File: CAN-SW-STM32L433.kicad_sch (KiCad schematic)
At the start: 37 parts, among them J1 H GND L, J2 TERM, J3 UART1, J4 SWLINK, J5 CENTER +12V, U1 STM32L433RCT3, U2 MCP2562-E-SN

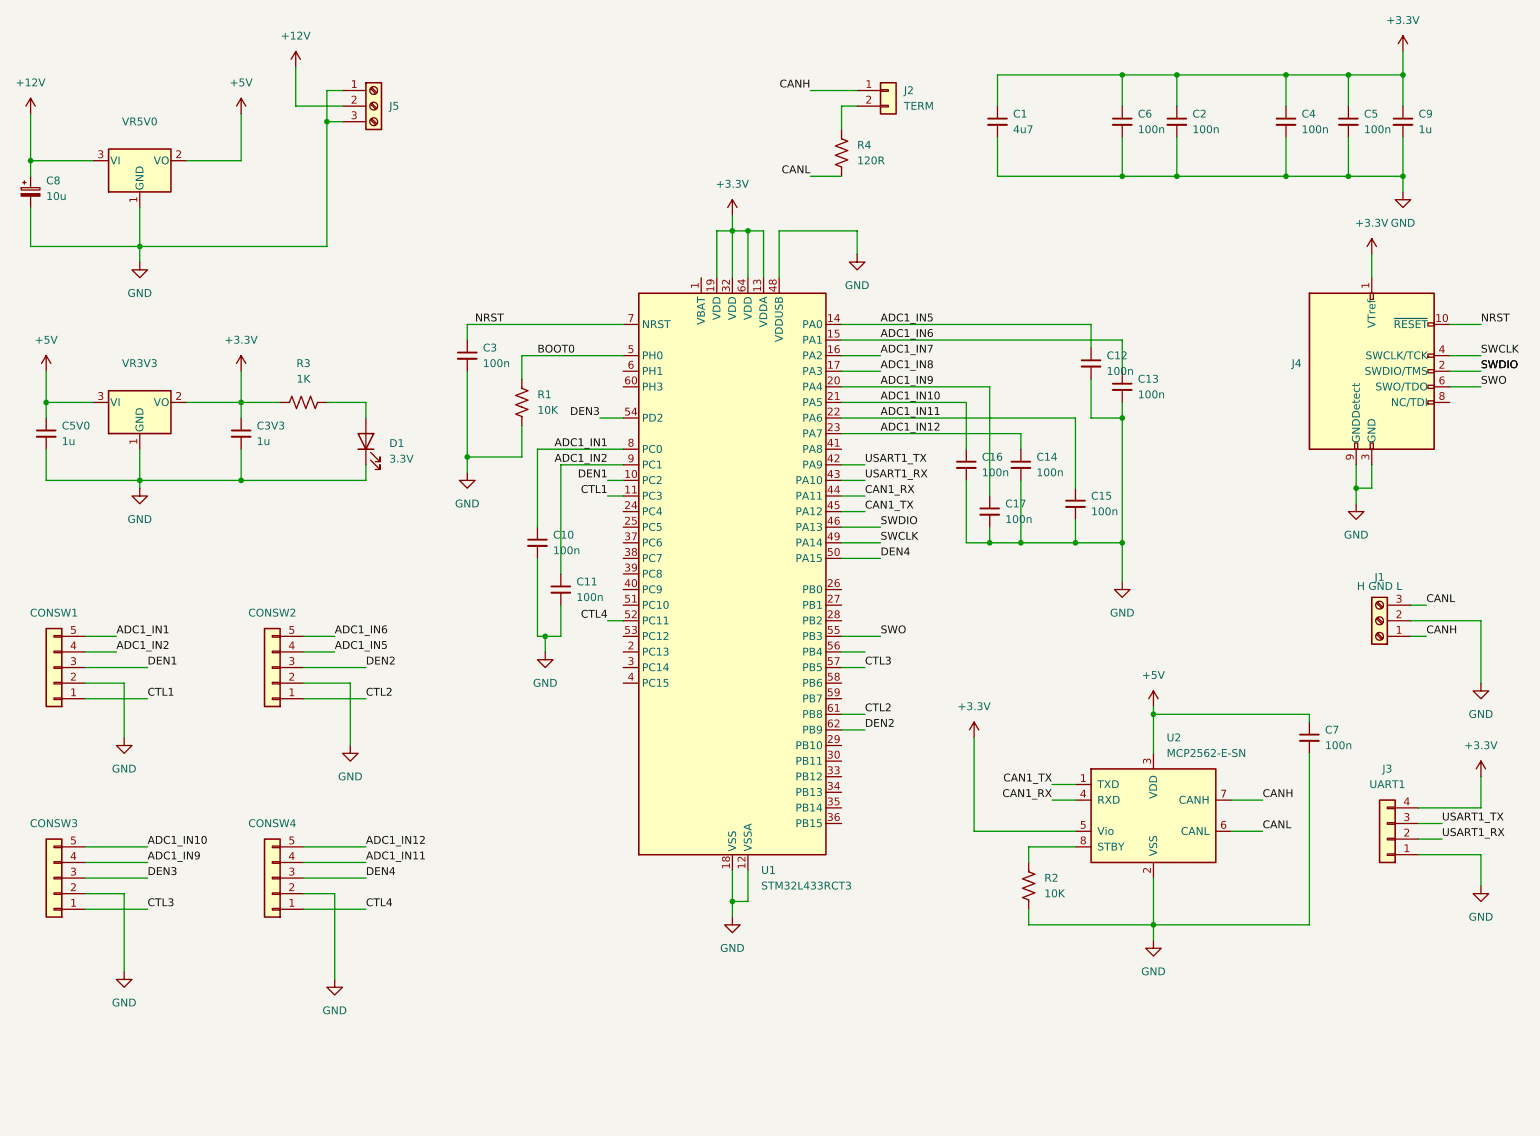
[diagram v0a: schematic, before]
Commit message: added status led and tvs diode
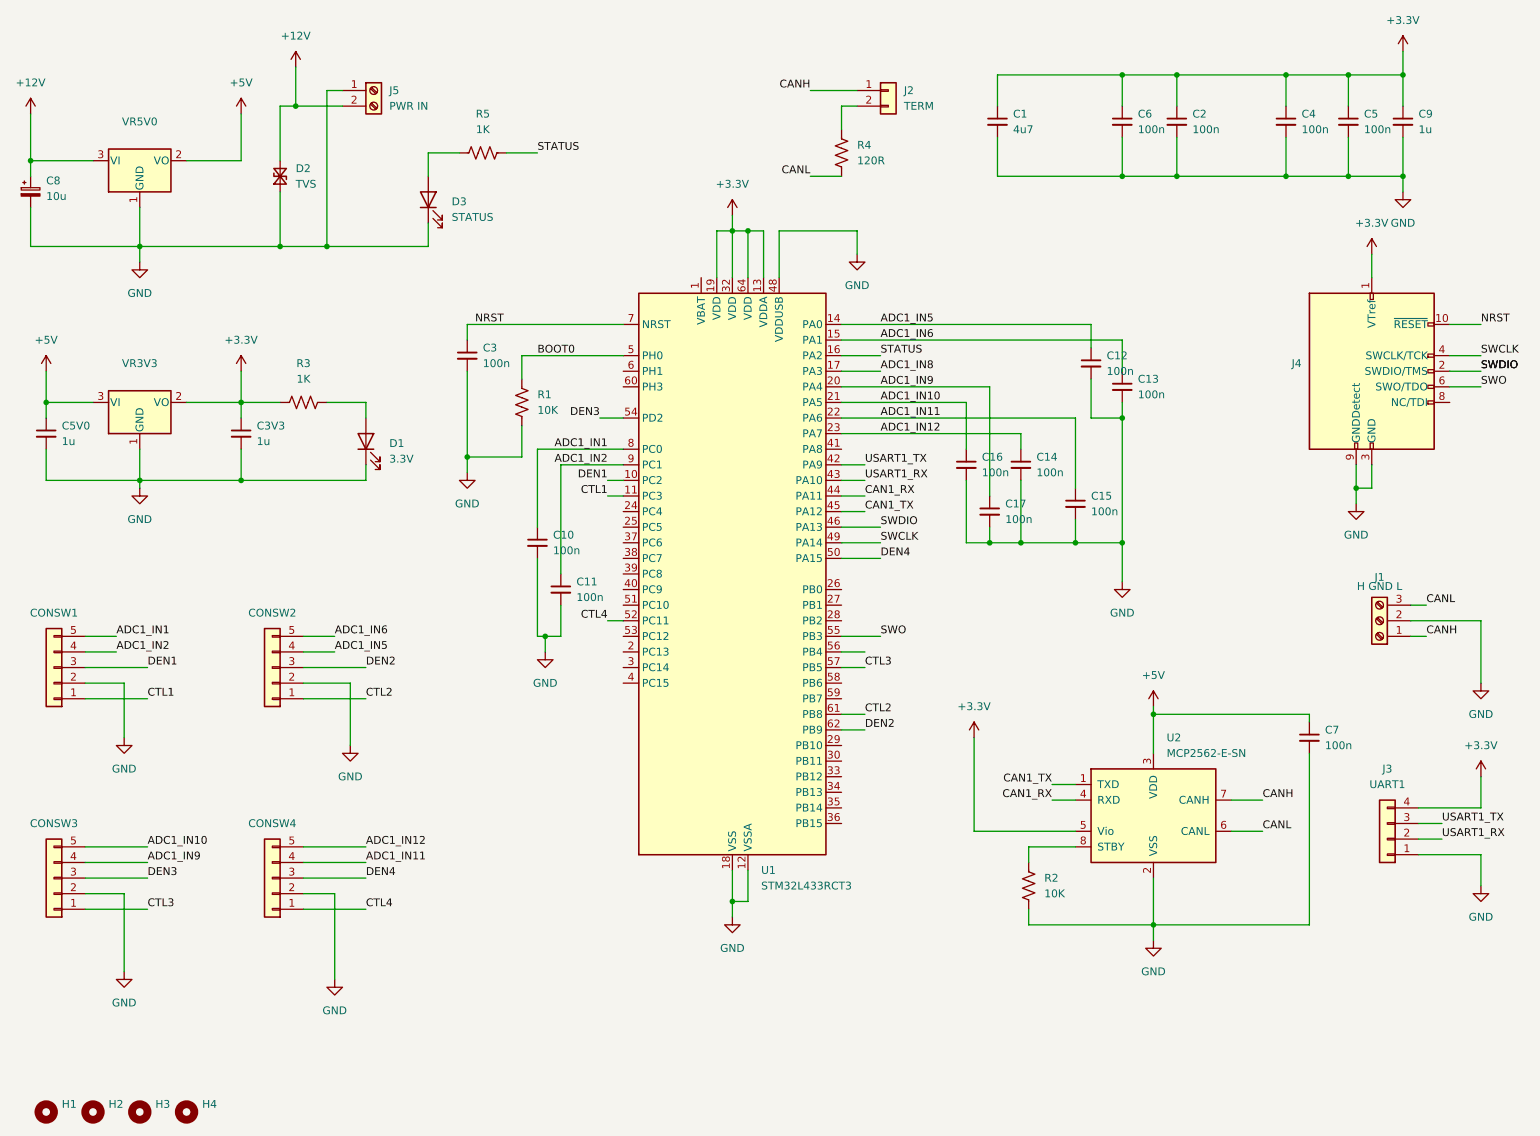
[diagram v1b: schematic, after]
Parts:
- removed J5: CENTER +12V, TerminalBlock_Phoenix:TerminalBlock_Phoenix_MKDS-1,5-3_1x03_P5.00mm_Horizontal, symbol Connector:Screw_Terminal_01x03
- added D2: TVS, Diode_SMD:D_0603_1608Metric_Pad1.05x0.95mm_HandSolder, symbol Device:D_TVS_Small
- added D3: STATUS, LED_THT:LED_D5.0mm_Clear, symbol Device:LED
- added H1, H2, H3, H4: MountingHole, MountingHole:MountingHole_3.2mm_M3_DIN965, symbol Mechanical:MountingHole
- added J5: PWR IN, TerminalBlock_Phoenix:TerminalBlock_Phoenix_MKDS-1,5-2_1x02_P5.00mm_Horizontal, symbol Connector:Screw_Terminal_01x02
- added R5: 1K, Resistor_SMD:R_0603_1608Metric_Pad0.98x0.95mm_HandSolder, symbol Device:R_US
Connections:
- net +12V: now also D2.2 (A2), J5.2 (Pin_2)
- net GND: now also D2.1 (A1), D3.1 (K), J5.1 (Pin_1)
- net ADC1_IN7 renamed STATUS
- net STATUS: now also R5.2
- new net: D3.2 (A), R5.1

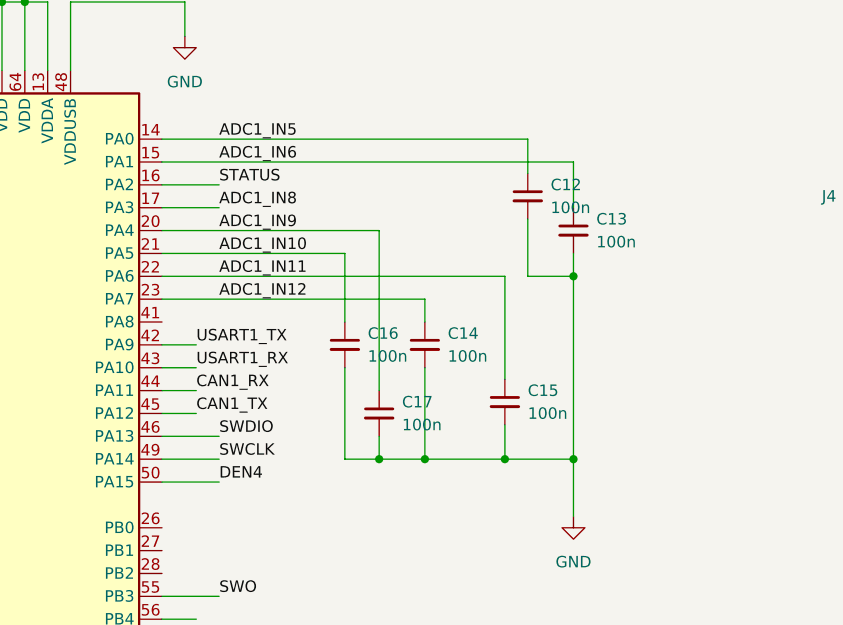
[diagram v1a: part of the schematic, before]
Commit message: fix TVS package size, do some layout tweaks
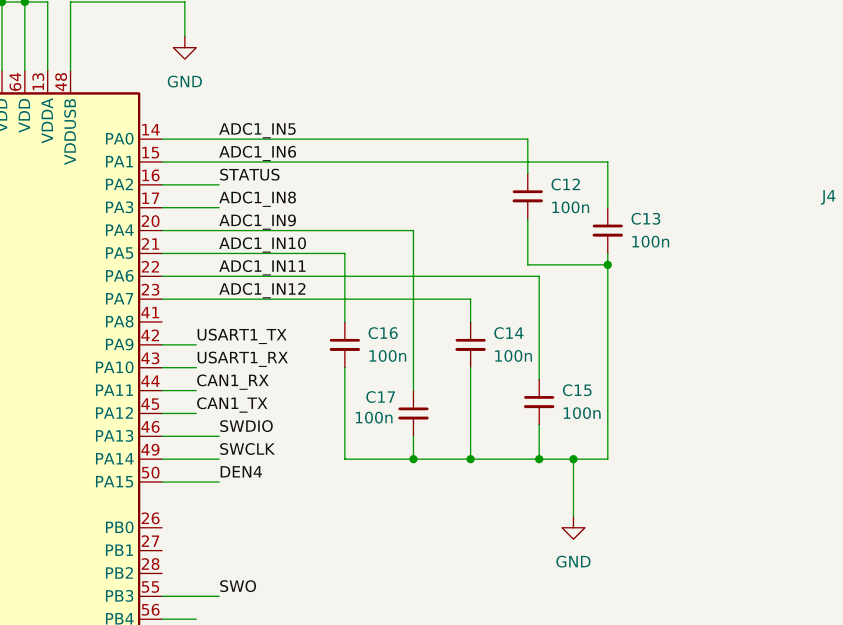
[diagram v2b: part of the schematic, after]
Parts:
- D2: footprint Diode_SMD:D_0603_1608Metric_Pad1.05x0.95mm_HandSolder -> Diode_SMD:D_SMA_Handsoldering
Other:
- moved on the sheet: C13, C14, C15, C17
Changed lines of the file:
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@@
 	)
 	(junction
-		(at 195.58 96.52)
+		(at 212.09 36.83)
 		(diameter 0)
 		(color 0 0 0 0)
 	)
 	(junction
-		(at 212.09 36.83)
+		(at 208.28 158.75)
 		(diameter 0)
 		(color 0 0 0 0)
 	)
 	(junction
-		(at 208.28 158.75)
+		(at 25.4 34.29)
 		(diameter 0)
 		(color 0 0 0 0)
 	)
 	(junction
-		(at 25.4 34.29)
+		(at 191.77 96.52)
 		(diameter 0)
 		(color 0 0 0 0)
@@
 	)
 	(junction
-		(at 68.58 25.4)
+		(at 185.42 96.52)
 		(diameter 0)
 		(color 0 0 0 0)
 	)
 	(junction
-		(at 186.69 96.52)
+		(at 68.58 25.4)
 		(diameter 0)
 		(color 0 0 0 0)
@@
 	)
 	(junction
+		(at 199.39 96.52)
+		(diameter 0)
+		(color 0 0 0 0)
+	)
+	(junction
 		(at 212.09 20.32)
 		(diameter 0)
@@
 	)
 	(junction
-		(at 181.61 96.52)
-		(diameter 0)
-		(color 0 0 0 0)
-	)
-	(junction
-		(at 203.2 76.2)
+		(at 207.01 74.93)
 		(diameter 0)
 		(color 0 0 0 0)
@@
 	(wire
 		(pts
-			(xy 181.61 71.12) (xy 181.61 88.9)
+			(xy 185.42 71.12) (xy 185.42 88.9)
 		)
 		(stroke
@@
 	(wire
 		(pts
-			(xy 203.2 73.66) (xy 203.2 76.2)
+			(xy 207.01 73.66) (xy 207.01 74.93)
 		)
 		(stroke
@@
 	(wire
 		(pts
+			(xy 191.77 96.52) (xy 199.39 96.52)
+		)
+		(stroke
+			(width 0)
+			(type default)
+		)
+	)
+	(wire
+		(pts
 			(xy 261.62 109.22) (xy 250.19 109.22)
 		)
@@
 	(wire
 		(pts
-			(xy 181.61 96.52) (xy 177.8 96.52)
+			(xy 177.8 96.52) (xy 185.42 96.52)
 		)
 		(stroke
@@
 	(wire
 		(pts
+			(xy 199.39 96.52) (xy 203.2 96.52)
+		)
+		(stroke
+			(width 0)
+			(type default)
+		)
+	)
+	(wire
+		(pts
 			(xy 157.48 124.46) (xy 161.29 124.46)
 		)
@@
 	(wire
 		(pts
+			(xy 207.01 96.52) (xy 203.2 96.52)
+		)
+		(stroke
+			(width 0)
+			(type default)
+		)
+	)
+	(wire
+		(pts
 			(xy 240.03 20.32) (xy 248.92 20.32)
 		)
@@
 	(wire
 		(pts
-			(xy 195.58 76.2) (xy 195.58 87.63)
+			(xy 199.39 76.2) (xy 199.39 87.63)
 		)
 		(stroke
@@
 	(wire
 		(pts
-			(xy 157.48 76.2) (xy 195.58 76.2)
+			(xy 157.48 76.2) (xy 199.39 76.2)
 		)
 		(stroke
@@
 	(wire
 		(pts
-			(xy 203.2 76.2) (xy 203.2 96.52)
-		)
-		(stroke
-			(width 0)
-			(type default)
-		)
-	)
-	(wire
-		(pts
 			(xy 147.32 53.34) (xy 147.32 45.72)
 		)
@@
 	(wire
 		(pts
-			(xy 157.48 78.74) (xy 186.69 78.74)
+			(xy 157.48 78.74) (xy 191.77 78.74)
 		)
 		(stroke
@@
 	(wire
 		(pts
-			(xy 195.58 92.71) (xy 195.58 96.52)
+			(xy 199.39 92.71) (xy 199.39 96.52)
 		)
 		(stroke
@@
 	(wire
 		(pts
+			(xy 185.42 96.52) (xy 191.77 96.52)
+		)
+		(stroke
+			(width 0)
+			(type default)
+		)
+	)
+	(wire
+		(pts
 			(xy 139.7 154.94) (xy 142.24 154.94)
 		)
@@
 	(wire
 		(pts
-			(xy 186.69 86.36) (xy 186.69 96.52)
+			(xy 191.77 86.36) (xy 191.77 96.52)
 		)
 		(stroke
@@
 	(wire
 		(pts
-			(xy 186.69 96.52) (xy 181.61 96.52)
-		)
-		(stroke
-			(width 0)
-			(type default)
-		)
-	)
-	(wire
-		(pts
 			(xy 40.64 153.67) (xy 40.64 166.37)
 		)
@@
 	(wire
 		(pts
-			(xy 198.12 76.2) (xy 203.2 76.2)
+			(xy 198.12 74.93) (xy 207.01 74.93)
 		)
 		(stroke
@@
 	(wire
 		(pts
-			(xy 157.48 71.12) (xy 181.61 71.12)
+			(xy 157.48 71.12) (xy 185.42 71.12)
 		)
 		(stroke
@@
 	(wire
 		(pts
-			(xy 186.69 78.74) (xy 186.69 81.28)
+			(xy 191.77 78.74) (xy 191.77 81.28)
 		)
 		(stroke
@@
 	(wire
 		(pts
-			(xy 181.61 93.98) (xy 181.61 96.52)
+			(xy 185.42 93.98) (xy 185.42 96.52)
 		)
 		(stroke
@@
 	(wire
 		(pts
-			(xy 198.12 69.85) (xy 198.12 76.2)
+			(xy 198.12 69.85) (xy 198.12 74.93)
 		)
 		(stroke
@@
 	(wire
 		(pts
-			(xy 195.58 96.52) (xy 203.2 96.52)
-		)
-		(stroke
-			(width 0)
-			(type default)
-		)
-	)
-	(wire
-		(pts
 			(xy 229.87 36.83) (xy 240.03 36.83)
 		)
@@
 	(wire
 		(pts
-			(xy 186.69 96.52) (xy 195.58 96.52)
+			(xy 207.01 74.93) (xy 207.01 96.52)
 		)
 		(stroke
@@
 	(wire
 		(pts
-			(xy 203.2 68.58) (xy 203.2 63.5)
+			(xy 207.01 68.58) (xy 207.01 63.5)
 		)
 		(stroke
@@
 	(wire
 		(pts
-			(xy 157.48 63.5) (xy 203.2 63.5)
+			(xy 157.48 63.5) (xy 207.01 63.5)
 		)
 		(stroke
@@
 	(symbol
 		(lib_id "Device:C_Small")
-		(at 203.2 71.12 0)
+		(at 207.01 71.12 0)
 		(unit 1)
 		(exclude_from_sim no)
@@
 		(on_board yes)
 		(dnp no)
-		(fields_autoplaced yes)
 		(property "Reference" "C13"
-			(at 205.74 69.8562 0)
+			(at 209.55 69.8562 0)
 			(effects
 				(font
@@
 		)
 		(property "Value" "100n"
-			(at 205.74 72.3962 0)
+			(at 209.55 72.3962 0)
 			(effects
 				(font
@@
 		)
 		(property "Footprint" "Capacitor_SMD:C_0603_1608Metric_Pad1.08x0.95mm_HandSolder"
-			(at 203.2 71.12 0)
+			(at 207.01 71.12 0)
 			(effects
 				(font
@@
 		)
 		(property "Datasheet" "~"
-			(at 203.2 71.12 0)
+			(at 207.01 71.12 0)
 			(effects
 				(font
@@
 		)
 		(property "Description" "Unpolarized capacitor, small symbol"
-			(at 203.2 71.12 0)
+			(at 207.01 71.12 0)
 			(effects
 				(font
@@
 	(symbol
 		(lib_id "Device:C_Small")
-		(at 186.69 83.82 0)
+		(at 191.77 83.82 0)
 		(unit 1)
 		(exclude_from_sim no)
@@
 		(dnp no)
 		(property "Reference" "C14"
-			(at 189.23 82.5562 0)
+			(at 194.31 82.5562 0)
 			(effects
 				(font
@@
 		)
 		(property "Value" "100n"
-			(at 189.23 85.0962 0)
+			(at 194.31 85.0962 0)
 			(effects
 				(font
@@
 		)
 		(property "Footprint" "Capacitor_SMD:C_0603_1608Metric_Pad1.08x0.95mm_HandSolder"
-			(at 186.69 83.82 0)
+			(at 191.77 83.82 0)
 			(effects
 				(font
@@
 		)
 		(property "Datasheet" "~"
-			(at 186.69 83.82 0)
+			(at 191.77 83.82 0)
 			(effects
 				(font
@@
 		)
 		(property "Description" "Unpolarized capacitor, small symbol"
-			(at 186.69 83.82 0)
+			(at 191.77 83.82 0)
 			(effects
 				(font
@@
 	(symbol
 		(lib_id "Device:C_Small")
-		(at 181.61 91.44 0)
+		(at 185.42 91.44 0)
 		(unit 1)
 		(exclude_from_sim no)
@@
 		(dnp no)
 		(property "Reference" "C17"
-			(at 184.15 90.1762 0)
+			(at 180.086 89.662 0)
 			(effects
 				(font
@@
 		)
 		(property "Value" "100n"
-			(at 184.15 92.7162 0)
+			(at 178.816 91.948 0)
 			(effects
 				(font
@@
 		)
 		(property "Footprint" "Capacitor_SMD:C_0603_1608Metric_Pad1.08x0.95mm_HandSolder"
-			(at 181.61 91.44 0)
+			(at 185.42 91.44 0)
 			(effects
 				(font
@@
 		)
 		(property "Datasheet" "~"
-			(at 181.61 91.44 0)
+			(at 185.42 91.44 0)
 			(effects
 				(font
@@
 		)
 		(property "Description" "Unpolarized capacitor, small symbol"
-			(at 181.61 91.44 0)
+			(at 185.42 91.44 0)
 			(effects
 				(font
@@
 			)
 		)
-		(property "Footprint" "Diode_SMD:D_0603_1608Metric_Pad1.05x0.95mm_HandSolder"
+		(property "Footprint" "Diode_SMD:D_SMA_Handsoldering"
 			(at 66.04 36.83 0)
 			(effects
@@
 	(symbol
 		(lib_id "Device:C_Small")
-		(at 195.58 90.17 0)
+		(at 199.39 90.17 0)
 		(unit 1)
 		(exclude_from_sim no)
@@
 		(fields_autoplaced yes)
 		(property "Reference" "C15"
-			(at 198.12 88.9062 0)
+			(at 201.93 88.9062 0)
 			(effects
 				(font
@@
 		)
 		(property "Value" "100n"
-			(at 198.12 91.4462 0)
+			(at 201.93 91.4462 0)
 			(effects
 				(font
@@
 		)
 		(property "Footprint" "Capacitor_SMD:C_0603_1608Metric_Pad1.08x0.95mm_HandSolder"
-			(at 195.58 90.17 0)
+			(at 199.39 90.17 0)
 			(effects
 				(font
@@
 		)
 		(property "Datasheet" "~"
-			(at 195.58 90.17 0)
+			(at 199.39 90.17 0)
 			(effects
 				(font
@@
 		)
 		(property "Description" "Unpolarized capacitor, small symbol"
-			(at 195.58 90.17 0)
+			(at 199.39 90.17 0)
 			(effects
 				(font
